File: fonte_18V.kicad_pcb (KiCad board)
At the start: 2 copper layers, 100 x 52 mm, 68 parts, among them J101 IN, J102 Conn_01x02, J401 RJ45_Shielded, J402 RJ45_Shielded, Q1 Si2308CDS, Q301 Si2308CDS, U1 LMR16030, U301 LMR16030

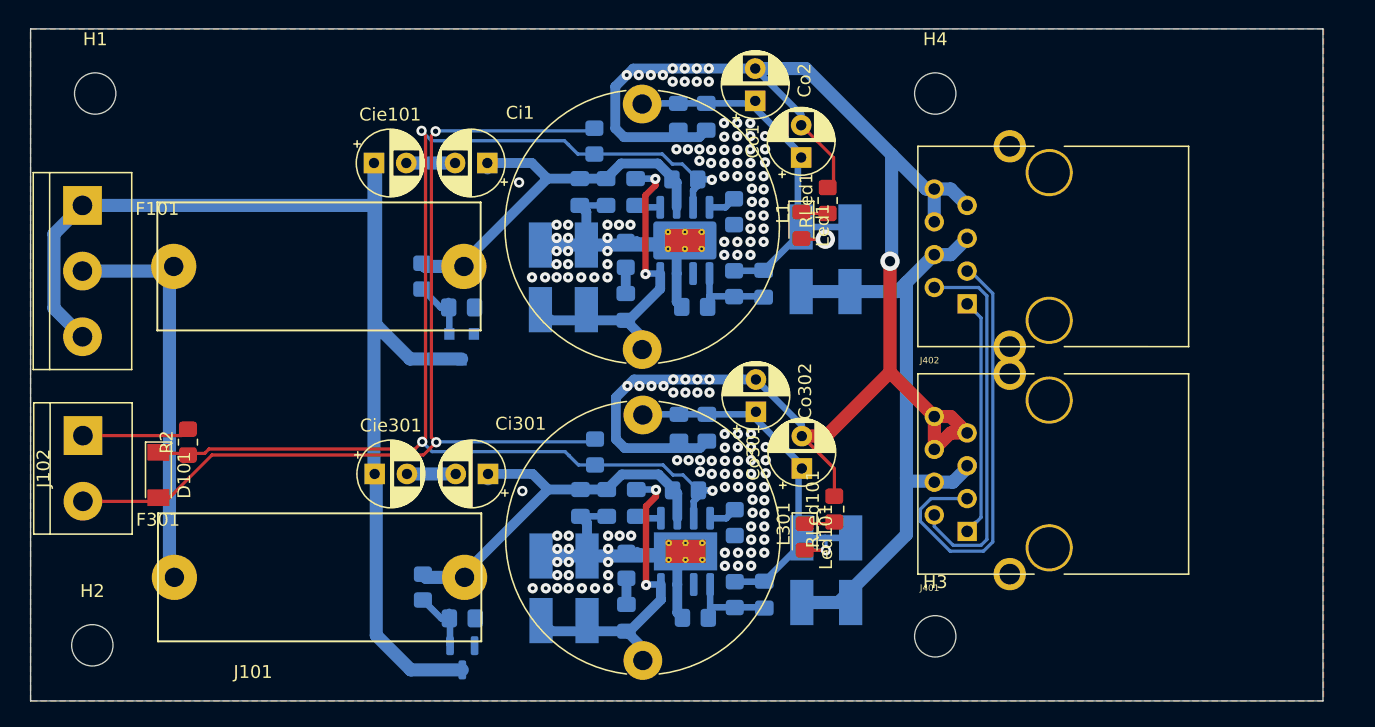
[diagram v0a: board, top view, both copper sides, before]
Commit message: Adjusted silkscreen and fixed RDC errors
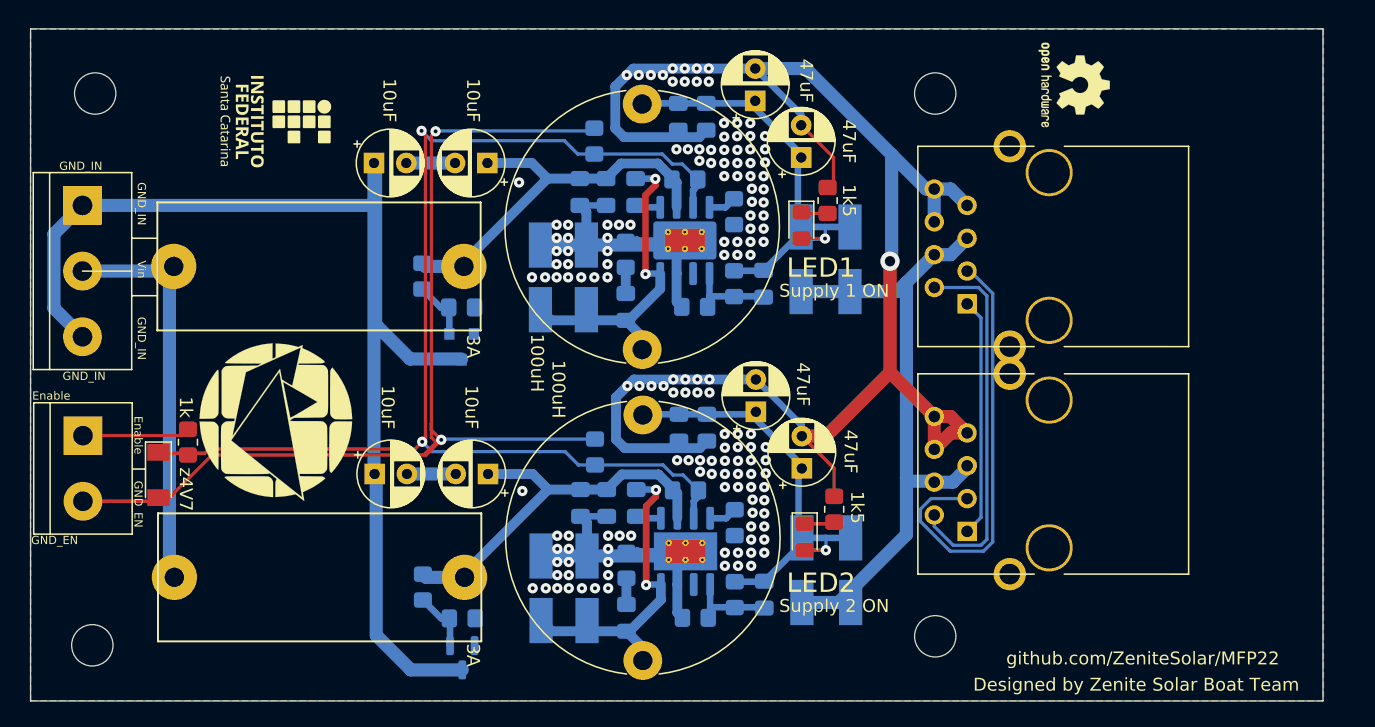
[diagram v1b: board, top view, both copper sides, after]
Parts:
- removed Led101: LED, LED_SMD:LED_0805_2012Metric_Pad1.15x1.40mm_HandSolder
- removed RLed101: 1k5, Resistor_SMD:R_0805_2012Metric_Pad1.20x1.40mm_HandSolder
- added LOGO101: Logo_Open_Hardware_Small, Symbol:OSHW-Logo2_7.3x6mm_SilkScreen, F.Cu at (103.1, 140.5)
- added Led2: LED, LED_SMD:LED_0805_2012Metric_Pad1.15x1.40mm_HandSolder, F.Cu at (82.3, 175.5)
- added RLed2: 1k5, Resistor_SMD:R_0805_2012Metric_Pad1.20x1.40mm_HandSolder, F.Cu at (84.6, 173.4)
- added SYM101: SYM_Flash_Small, KicadZeniteSolarLibrary18:symbol_logoZenite, B.Cu at (41.4, 166.2)
- added SYM102: SYM_Flash_Small, KicadZeniteSolarLibrary18:symbol_logoZenite, F.Cu at (41.4, 166.6)
- added SYM103: SYM_Flash_Small, KicadZeniteSolarLibrary18:synbol_logoifsc, F.Cu at (41.4, 143.4)
- added SYM104: SYM_Flash_Small, KicadZeniteSolarLibrary18:synbol_logoifsc, B.Cu at (41.4, 143.4)
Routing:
- net GND: track 291.8 -> 294.7 mm
- net Net-(Led2-Pad1): track 0.00 -> 2.34 mm
- net Net-(Led101-Pad1): track 2.34 -> 0.00 mm
- net /EN: track 97.4 -> 95.1 mm, vias 4 -> 2
- net Net-(J401-Pad1): track 20.3 -> 18.5 mm
- net /supply1/IN: track 31.1 -> 30.6 mm
- net Net-(Q301-Pad1): track 5.28 -> 4.77 mm
- net Net-(Q1-Pad1): track 5.28 -> 4.77 mm
- net Net-(Ci301-Pad1): track 31.5 -> 31.0 mm
- net Net-(Ci1-Pad1): track 31.5 -> 31.0 mm
- net /supply1/CAN_18V_DIODE: track 35.1 -> 35.3 mm, vias 2 -> 1
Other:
- board text added: "+18V"
- board text added: "100k"
- board text added: "100nF"
- board text added: "100uH"
- board text added: "10k"
- board text added: "10uF"
- board text added: "1k"
- board text added: "1k5"
- board text added: "220k"
- board text added: "230k"
- board text added: "2k2"
- board text added: "3A"
- board text added: "47k"
- board text added: "47uF"
- board text added: "8k2"
- board text added: "B1100"
- board text added: "Designed by Zenite Solar Boat Team"
- board text added: "Enable"
- board text added: "GND"
- board text added: "GND_EN"
- board text added: "GND_IN"
- board text added: "LED1"
- board text added: "LED2"
- board text added: "MBR340"
- board text added: "Si2308CDS"
- board text added: "Supply 1 ON"
- board text added: "Supply 2 ON"
- board text added: "Vin"
- board text added: "github.com/ZeniteSolar/MFP22"
- board text added: "z4V7"
